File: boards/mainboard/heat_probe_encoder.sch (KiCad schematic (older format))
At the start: 27 parts, among them U1201 DB_26, U1202 DS26LV32AT, U1203 DS26LV32AT

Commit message: [mainboard] update connectors, select most footprints; docs: update SVGs
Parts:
- C1201, C1202, C1203, C1204, C1205, C1206: footprint (none) -> Capacitors_SMD:C_0603
- R1201, R1202, R1203, R1204, R1205, R1206, R1207, R1208, R1209, R1210, R1211, R1212, R1213, R1214, R1215, R1216, R1217, R1218: footprint (none) -> Resistors_SMD:R_0603
- U1202, U1203: footprint (none) -> Housings_SOIC:SOIC-16_3.9x9.9mm_Pitch1.27mm
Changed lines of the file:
@@
 $EndDescr
 $Comp
-L GND #PWR1202
+L GND #PWR0119
 U 1 1 591E0FA6
 P 1650 4900
-F 0 "#PWR1202" H 1650 4650 50  0001 C CNN
+F 0 "#PWR0119" H 1650 4650 50  0001 C CNN
 F 1 "GND" H 1650 4750 50  0000 C CNN
 F 2 "" H 1650 4900 50  0001 C CNN
@@
 F 0 "R1213" V 8080 2400 50  0000 C CNN
 F 1 "100" V 8000 2400 50  0000 C CNN
-F 2 "" V 7930 2400 50  0001 C CNN
+F 2 "Resistors_SMD:R_0603" V 7930 2400 50  0001 C CNN
 F 3 "" H 8000 2400 50  0001 C CNN
 	1    8000 2400
@@
 F 0 "R1214" V 8080 2600 50  0000 C CNN
 F 1 "100" V 8000 2600 50  0000 C CNN
-F 2 "" V 7930 2600 50  0001 C CNN
+F 2 "Resistors_SMD:R_0603" V 7930 2600 50  0001 C CNN
 F 3 "" H 8000 2600 50  0001 C CNN
 	1    8000 2600
@@
 F 0 "R1215" V 8080 2800 50  0000 C CNN
 F 1 "100" V 8000 2800 50  0000 C CNN
-F 2 "" V 7930 2800 50  0001 C CNN
+F 2 "Resistors_SMD:R_0603" V 7930 2800 50  0001 C CNN
 F 3 "" H 8000 2800 50  0001 C CNN
 	1    8000 2800
@@
 F 0 "R1216" V 8080 3000 50  0000 C CNN
 F 1 "100" V 8000 3000 50  0000 C CNN
-F 2 "" V 7930 3000 50  0001 C CNN
+F 2 "Resistors_SMD:R_0603" V 7930 3000 50  0001 C CNN
 F 3 "" H 8000 3000 50  0001 C CNN
 	1    8000 3000
@@
 F 0 "R1217" V 8080 3200 50  0000 C CNN
 F 1 "100" V 8000 3200 50  0000 C CNN
-F 2 "" V 7930 3200 50  0001 C CNN
+F 2 "Resistors_SMD:R_0603" V 7930 3200 50  0001 C CNN
 F 3 "" H 8000 3200 50  0001 C CNN
 	1    8000 3200
@@
 F 0 "R1218" V 8080 3400 50  0000 C CNN
 F 1 "100" V 8000 3400 50  0000 C CNN
-F 2 "" V 7930 3400 50  0001 C CNN
+F 2 "Resistors_SMD:R_0603" V 7930 3400 50  0001 C CNN
 F 3 "" H 8000 3400 50  0001 C CNN
 	1    8000 3400
@@
 F 0 "C1201" H 8325 3800 50  0000 L CNN
 F 1 "2n7" H 8325 3600 50  0000 L CNN
-F 2 "" H 8338 3550 50  0001 C CNN
+F 2 "Capacitors_SMD:C_0603" H 8338 3550 50  0001 C CNN
 F 3 "" H 8300 3700 50  0001 C CNN
 	1    8300 3700
@@
 F 0 "C1202" H 8575 3800 50  0000 L CNN
 F 1 "2n7" H 8575 3600 50  0000 L CNN
-F 2 "" H 8588 3550 50  0001 C CNN
+F 2 "Capacitors_SMD:C_0603" H 8588 3550 50  0001 C CNN
 F 3 "" H 8550 3700 50  0001 C CNN
 	1    8550 3700
@@
 F 0 "C1203" H 8825 3800 50  0000 L CNN
 F 1 "2n7" H 8825 3600 50  0000 L CNN
-F 2 "" H 8838 3550 50  0001 C CNN
+F 2 "Capacitors_SMD:C_0603" H 8838 3550 50  0001 C CNN
 F 3 "" H 8800 3700 50  0001 C CNN
 	1    8800 3700
@@
 F 0 "C1204" H 9075 3800 50  0000 L CNN
 F 1 "2n7" H 9075 3600 50  0000 L CNN
-F 2 "" H 9088 3550 50  0001 C CNN
+F 2 "Capacitors_SMD:C_0603" H 9088 3550 50  0001 C CNN
 F 3 "" H 9050 3700 50  0001 C CNN
 	1    9050 3700
@@
 F 0 "C1205" H 9325 3800 50  0000 L CNN
 F 1 "2n7" H 9325 3600 50  0000 L CNN
-F 2 "" H 9338 3550 50  0001 C CNN
+F 2 "Capacitors_SMD:C_0603" H 9338 3550 50  0001 C CNN
 F 3 "" H 9300 3700 50  0001 C CNN
 	1    9300 3700
@@
 F 0 "C1206" H 9575 3800 50  0000 L CNN
 F 1 "2n7" H 9575 3600 50  0000 L CNN
-F 2 "" H 9588 3550 50  0001 C CNN
+F 2 "Capacitors_SMD:C_0603" H 9588 3550 50  0001 C CNN
 F 3 "" H 9550 3700 50  0001 C CNN
 	1    9550 3700
@@
 $EndComp
 $Comp
-L GND #PWR1212
+L GND #PWR0120
 U 1 1 591E1E04
 P 8300 4050
-F 0 "#PWR1212" H 8300 3800 50  0001 C CNN
+F 0 "#PWR0120" H 8300 3800 50  0001 C CNN
 F 1 "GND" H 8300 3900 50  0000 C CNN
 F 2 "" H 8300 4050 50  0001 C CNN
@@
 F 0 "R1212" V 7480 2050 50  0000 C CNN
 F 1 "2k7" V 7400 2050 50  0000 C CNN
-F 2 "" V 7330 2050 50  0001 C CNN
+F 2 "Resistors_SMD:R_0603" V 7330 2050 50  0001 C CNN
 F 3 "" H 7400 2050 50  0001 C CNN
 	1    7400 2050
@@
 F 0 "R1211" V 7280 2050 50  0000 C CNN
 F 1 "2k7" V 7200 2050 50  0000 C CNN
-F 2 "" V 7130 2050 50  0001 C CNN
+F 2 "Resistors_SMD:R_0603" V 7130 2050 50  0001 C CNN
 F 3 "" H 7200 2050 50  0001 C CNN
 	1    7200 2050
@@
 F 0 "R1210" V 7080 2050 50  0000 C CNN
 F 1 "2k7" V 7000 2050 50  0000 C CNN
-F 2 "" V 6930 2050 50  0001 C CNN
+F 2 "Resistors_SMD:R_0603" V 6930 2050 50  0001 C CNN
 F 3 "" H 7000 2050 50  0001 C CNN
 	1    7000 2050
@@
 F 0 "R1209" V 6880 2050 50  0000 C CNN
 F 1 "2k7" V 6800 2050 50  0000 C CNN
-F 2 "" V 6730 2050 50  0001 C CNN
+F 2 "Resistors_SMD:R_0603" V 6730 2050 50  0001 C CNN
 F 3 "" H 6800 2050 50  0001 C CNN
 	1    6800 2050
@@
 F 0 "R1208" V 6680 2050 50  0000 C CNN
 F 1 "2k7" V 6600 2050 50  0000 C CNN
-F 2 "" V 6530 2050 50  0001 C CNN
+F 2 "Resistors_SMD:R_0603" V 6530 2050 50  0001 C CNN
 F 3 "" H 6600 2050 50  0001 C CNN
 	1    6600 2050
@@
 F 0 "R1207" V 6480 2050 50  0000 C CNN
 F 1 "2k7" V 6400 2050 50  0000 C CNN
-F 2 "" V 6330 2050 50  0001 C CNN
+F 2 "Resistors_SMD:R_0603" V 6330 2050 50  0001 C CNN
 F 3 "" H 6400 2050 50  0001 C CNN
 	1    6400 2050
@@
 $EndComp
 $Comp
-L +3V3 #PWR1211
+L +3V3 #PWR0121
 U 1 1 591E2628
 P 6900 1700
-F 0 "#PWR1211" H 6900 1550 50  0001 C CNN
+F 0 "#PWR0121" H 6900 1550 50  0001 C CNN
 F 1 "+3V3" H 6900 1840 50  0000 C CNN
 F 2 "" H 6900 1700 50  0001 C CNN
@@
 F 0 "U1202" H 5450 3550 60  0000 C CNN
 F 1 "DS26LV32AT" H 5450 4650 60  0000 C CNN
-F 2 "" H 5550 3900 60  0001 C CNN
+F 2 "Housings_SOIC:SOIC-16_3.9x9.9mm_Pitch1.27mm" H 5550 3900 60  0001 C CNN
 F 3 "" H 5550 3900 60  0001 C CNN
 	1    5450 4100
@@
 $EndComp
 $Comp
-L +5V #PWR1201
+L +5V #PWR0122
 U 1 1 591E0FAC
 P 1550 1900
-F 0 "#PWR1201" H 1550 1750 50  0001 C CNN
+F 0 "#PWR0122" H 1550 1750 50  0001 C CNN
 F 1 "+5V" H 1550 2040 50  0000 C CNN
 F 2 "" H 1550 1900 50  0000 C CNN
@@
 F 0 "R1201" V 4680 2400 50  0000 C CNN
 F 1 "0" V 4600 2400 50  0000 C CNN
-F 2 "" V 4530 2400 50  0001 C CNN
+F 2 "Resistors_SMD:R_0603" V 4530 2400 50  0001 C CNN
 F 3 "" H 4600 2400 50  0001 C CNN
 	1    4600 2400
@@
 F 0 "R1202" V 4680 2600 50  0000 C CNN
 F 1 "0" V 4600 2600 50  0000 C CNN
-F 2 "" V 4530 2600 50  0001 C CNN
+F 2 "Resistors_SMD:R_0603" V 4530 2600 50  0001 C CNN
 F 3 "" H 4600 2600 50  0001 C CNN
 	1    4600 2600
@@
 F 0 "R1203" V 4680 2800 50  0000 C CNN
 F 1 "0" V 4600 2800 50  0000 C CNN
-F 2 "" V 4530 2800 50  0001 C CNN
+F 2 "Resistors_SMD:R_0603" V 4530 2800 50  0001 C CNN
 F 3 "" H 4600 2800 50  0001 C CNN
 	1    4600 2800
@@
 F 0 "R1204" V 4680 3000 50  0000 C CNN
 F 1 "0" V 4600 3000 50  0000 C CNN
-F 2 "" V 4530 3000 50  0001 C CNN
+F 2 "Resistors_SMD:R_0603" V 4530 3000 50  0001 C CNN
 F 3 "" H 4600 3000 50  0001 C CNN
 	1    4600 3000
@@
 F 0 "R1205" V 4680 3200 50  0000 C CNN
 F 1 "0" V 4600 3200 50  0000 C CNN
-F 2 "" V 4530 3200 50  0001 C CNN
+F 2 "Resistors_SMD:R_0603" V 4530 3200 50  0001 C CNN
 F 3 "" H 4600 3200 50  0001 C CNN
 	1    4600 3200
@@
 F 0 "R1206" V 4680 3400 50  0000 C CNN
 F 1 "0" V 4600 3400 50  0000 C CNN
-F 2 "" V 4530 3400 50  0001 C CNN
+F 2 "Resistors_SMD:R_0603" V 4530 3400 50  0001 C CNN
 F 3 "" H 4600 3400 50  0001 C CNN
 	1    4600 3400
@@
 $EndComp
 $Comp
-L +3V3 #PWR1207
+L +3V3 #PWR0123
 U 1 1 591F1091
 P 6050 4450
-F 0 "#PWR1207" H 6050 4300 50  0001 C CNN
+F 0 "#PWR0123" H 6050 4300 50  0001 C CNN
 F 1 "+3V3" H 6050 4590 50  0000 C CNN
 F 2 "" H 6050 4450 50  0001 C CNN
@@
 $EndComp
 $Comp
-L GND #PWR1208
+L GND #PWR0124
 U 1 1 591F1111
 P 6050 4650
-F 0 "#PWR1208" H 6050 4400 50  0001 C CNN
+F 0 "#PWR0124" H 6050 4400 50  0001 C CNN
 F 1 "GND" H 6050 4500 50  0000 C CNN
 F 2 "" H 6050 4650 50  0001 C CNN
@@
 $EndComp
 $Comp
-L GND #PWR1204
+L GND #PWR0125
 U 1 1 591F1174
 P 4850 4650
-F 0 "#PWR1204" H 4850 4400 50  0001 C CNN
+F 0 "#PWR0125" H 4850 4400 50  0001 C CNN
 F 1 "GND" H 4850 4500 50  0000 C CNN
 F 2 "" H 4850 4650 50  0001 C CNN
@@
 $EndComp
 $Comp
-L +3V3 #PWR1203
+L +3V3 #PWR0126
 U 1 1 591F11D0
 P 4850 4450
-F 0 "#PWR1203" H 4850 4300 50  0001 C CNN
+F 0 "#PWR0126" H 4850 4300 50  0001 C CNN
 F 1 "+3V3" H 4850 4590 50  0000 C CNN
 F 2 "" H 4850 4450 50  0001 C CNN
@@
 F 0 "U1203" H 5450 5000 60  0000 C CNN
 F 1 "DS26LV32AT" H 5450 6100 60  0000 C CNN
-F 2 "" H 5550 5350 60  0001 C CNN
+F 2 "Housings_SOIC:SOIC-16_3.9x9.9mm_Pitch1.27mm" H 5550 5350 60  0001 C CNN
 F 3 "" H 5550 5350 60  0001 C CNN
 	1    5450 5550
@@
 Connection ~ 3100 3400
 $Comp
-L GND #PWR1206
+L GND #PWR0127
 U 1 1 591F578A
 P 4850 6100
-F 0 "#PWR1206" H 4850 5850 50  0001 C CNN
+F 0 "#PWR0127" H 4850 5850 50  0001 C CNN
 F 1 "GND" H 4850 5950 50  0000 C CNN
 F 2 "" H 4850 6100 50  0001 C CNN
@@
 $EndComp
 $Comp
-L +3V3 #PWR1205
+L +3V3 #PWR0128
 U 1 1 591F5790
 P 4850 5900
-F 0 "#PWR1205" H 4850 5750 50  0001 C CNN
+F 0 "#PWR0128" H 4850 5750 50  0001 C CNN
 F 1 "+3V3" H 4850 6040 50  0000 C CNN
 F 2 "" H 4850 5900 50  0001 C CNN
@@
 	4850 6000 4850 6100
 $Comp
-L +3V3 #PWR1209
+L +3V3 #PWR0129
 U 1 1 591F5B8B
 P 6050 5900
-F 0 "#PWR1209" H 6050 5750 50  0001 C CNN
+F 0 "#PWR0129" H 6050 5750 50  0001 C CNN
 F 1 "+3V3" H 6050 6040 50  0000 C CNN
 F 2 "" H 6050 5900 50  0001 C CNN
@@
 $EndComp
 $Comp
-L GND #PWR1210
+L GND #PWR0130
 U 1 1 591F5B91
 P 6050 6100
-F 0 "#PWR1210" H 6050 5850 50  0001 C CNN
+F 0 "#PWR0130" H 6050 5850 50  0001 C CNN
 F 1 "GND" H 6050 5950 50  0000 C CNN
 F 2 "" H 6050 6100 50  0001 C CNN

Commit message: [mainboard] layout: footprints assigned, first placement
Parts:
- U1201: value DB_26 -> Heat probe encoder; footprint (none) -> D-Sub-HD:D-Sub_HD_26_F
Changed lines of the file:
@@
 $EndDescr
 $Comp
-L GND #PWR0119
+L GND #PWR0117
 U 1 1 591E0FA6
 P 1650 4900
-F 0 "#PWR0119" H 1650 4650 50  0001 C CNN
+F 0 "#PWR0117" H 1650 4650 50  0001 C CNN
 F 1 "GND" H 1650 4750 50  0000 C CNN
 F 2 "" H 1650 4900 50  0001 C CNN
@@
 $EndComp
 $Comp
-L GND #PWR0120
+L GND #PWR0118
 U 1 1 591E1E04
 P 8300 4050
-F 0 "#PWR0120" H 8300 3800 50  0001 C CNN
+F 0 "#PWR0118" H 8300 3800 50  0001 C CNN
 F 1 "GND" H 8300 3900 50  0000 C CNN
 F 2 "" H 8300 4050 50  0001 C CNN
@@
 $EndComp
 $Comp
-L +3V3 #PWR0121
+L +3V3 #PWR0119
 U 1 1 591E2628
 P 6900 1700
-F 0 "#PWR0121" H 6900 1550 50  0001 C CNN
+F 0 "#PWR0119" H 6900 1550 50  0001 C CNN
 F 1 "+3V3" H 6900 1840 50  0000 C CNN
 F 2 "" H 6900 1700 50  0001 C CNN
@@
 P 1050 3300
 F 0 "U1201" H 1050 1950 60  0000 C CNN
-F 1 "DB_26" H 1050 4750 60  0000 C CNN
-F 2 "" H 2250 3300 60  0001 C CNN
+F 1 "Heat probe encoder" H 1050 4750 60  0000 C CNN
+F 2 "D-Sub-HD:D-Sub_HD_26_F" H 2250 3300 60  0001 C CNN
 F 3 "" H 2250 3300 60  0001 C CNN
 	1    1050 3300
@@
 $EndComp
 $Comp
-L +5V #PWR0122
+L +5V #PWR0120
 U 1 1 591E0FAC
 P 1550 1900
-F 0 "#PWR0122" H 1550 1750 50  0001 C CNN
+F 0 "#PWR0120" H 1550 1750 50  0001 C CNN
 F 1 "+5V" H 1550 2040 50  0000 C CNN
 F 2 "" H 1550 1900 50  0000 C CNN
@@
 $EndComp
 $Comp
-L +3V3 #PWR0123
+L +3V3 #PWR0121
 U 1 1 591F1091
 P 6050 4450
-F 0 "#PWR0123" H 6050 4300 50  0001 C CNN
+F 0 "#PWR0121" H 6050 4300 50  0001 C CNN
 F 1 "+3V3" H 6050 4590 50  0000 C CNN
 F 2 "" H 6050 4450 50  0001 C CNN
@@
 $EndComp
 $Comp
-L GND #PWR0124
+L GND #PWR0122
 U 1 1 591F1111
 P 6050 4650
-F 0 "#PWR0124" H 6050 4400 50  0001 C CNN
+F 0 "#PWR0122" H 6050 4400 50  0001 C CNN
 F 1 "GND" H 6050 4500 50  0000 C CNN
 F 2 "" H 6050 4650 50  0001 C CNN
@@
 $EndComp
 $Comp
-L GND #PWR0125
+L GND #PWR0123
 U 1 1 591F1174
 P 4850 4650
-F 0 "#PWR0125" H 4850 4400 50  0001 C CNN
+F 0 "#PWR0123" H 4850 4400 50  0001 C CNN
 F 1 "GND" H 4850 4500 50  0000 C CNN
 F 2 "" H 4850 4650 50  0001 C CNN
@@
 $EndComp
 $Comp
-L +3V3 #PWR0126
+L +3V3 #PWR0124
 U 1 1 591F11D0
 P 4850 4450
-F 0 "#PWR0126" H 4850 4300 50  0001 C CNN
+F 0 "#PWR0124" H 4850 4300 50  0001 C CNN
 F 1 "+3V3" H 4850 4590 50  0000 C CNN
 F 2 "" H 4850 4450 50  0001 C CNN
@@
 Connection ~ 3100 3400
 $Comp
-L GND #PWR0127
+L GND #PWR0125
 U 1 1 591F578A
 P 4850 6100
-F 0 "#PWR0127" H 4850 5850 50  0001 C CNN
+F 0 "#PWR0125" H 4850 5850 50  0001 C CNN
 F 1 "GND" H 4850 5950 50  0000 C CNN
 F 2 "" H 4850 6100 50  0001 C CNN
@@
 $EndComp
 $Comp
-L +3V3 #PWR0128
+L +3V3 #PWR0126
 U 1 1 591F5790
 P 4850 5900
-F 0 "#PWR0128" H 4850 5750 50  0001 C CNN
+F 0 "#PWR0126" H 4850 5750 50  0001 C CNN
 F 1 "+3V3" H 4850 6040 50  0000 C CNN
 F 2 "" H 4850 5900 50  0001 C CNN
@@
 	4850 6000 4850 6100
 $Comp
-L +3V3 #PWR0129
+L +3V3 #PWR0127
 U 1 1 591F5B8B
 P 6050 5900
-F 0 "#PWR0129" H 6050 5750 50  0001 C CNN
+F 0 "#PWR0127" H 6050 5750 50  0001 C CNN
 F 1 "+3V3" H 6050 6040 50  0000 C CNN
 F 2 "" H 6050 5900 50  0001 C CNN
@@
 $EndComp
 $Comp
-L GND #PWR0130
+L GND #PWR0128
 U 1 1 591F5B91
 P 6050 6100
-F 0 "#PWR0130" H 6050 5850 50  0001 C CNN
+F 0 "#PWR0128" H 6050 5850 50  0001 C CNN
 F 1 "GND" H 6050 5950 50  0000 C CNN
 F 2 "" H 6050 6100 50  0001 C CNN

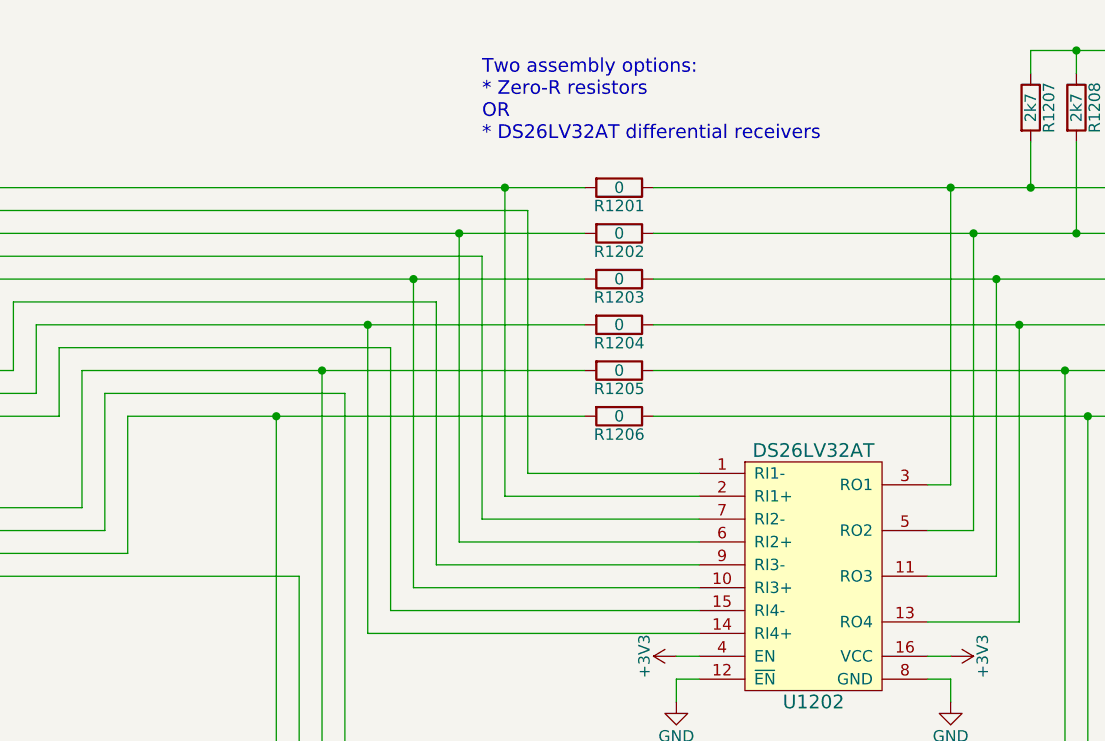
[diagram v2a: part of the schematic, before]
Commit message: [mainboard] layout: footprint placement
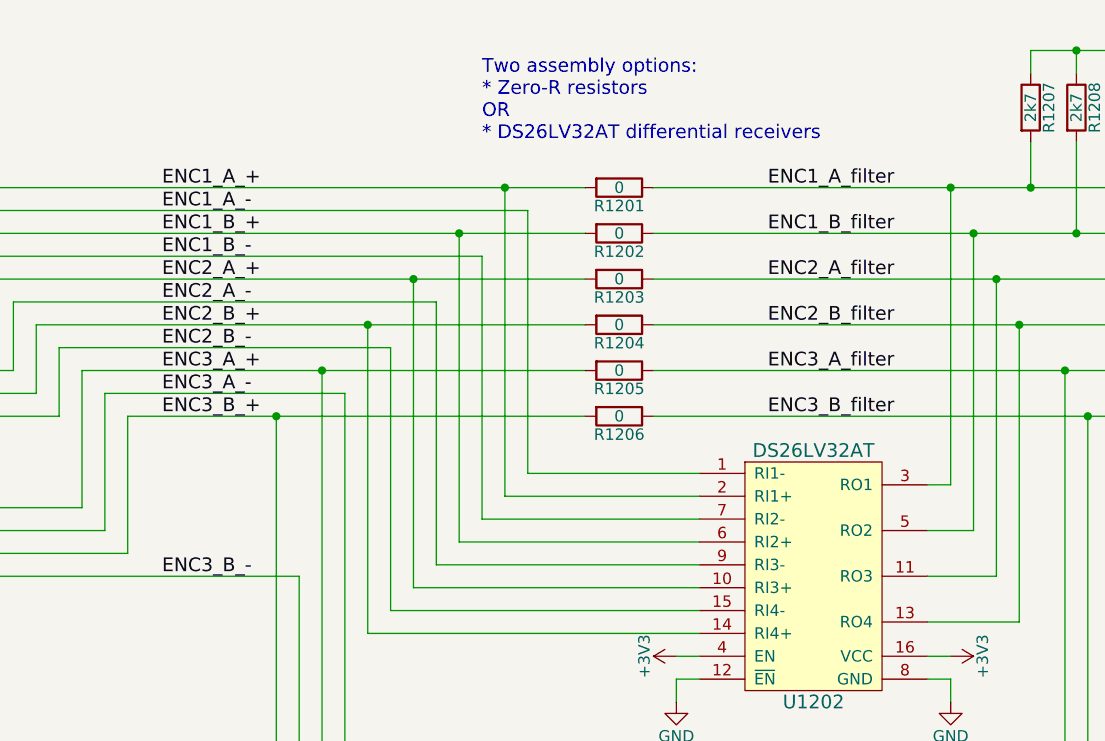
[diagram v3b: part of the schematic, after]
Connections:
- net ENC1_A_filter: now reaches R1201.1, R1207.2, R1213.2, U1202.3 (RO1)
- net ENC1_B_filter: now reaches R1202.1, R1208.2, R1214.2, U1202.5 (RO2)
- net ENC2_A_filter: now reaches R1203.1, R1209.2, R1215.2, U1202.11 (RO3)
- net ENC2_B_filter: now reaches R1204.1, R1210.2, R1216.2, U1202.13 (RO4)
- net ENC3_A_filter: now reaches R1205.1, R1211.2, R1217.2, U1203.3 (RO1)
- net ENC3_B_filter: now reaches R1206.1, R1212.2, R1218.2, U1203.5 (RO2)
- net ENC1_A_-: now reaches U1201.20, U1202.1 (RI1-)
- net ENC2_A_+: now reaches R1203.2, U1201.22, U1202.10 (RI3+)
- net ENC2_B_+: now reaches R1204.2, U1201.5, U1202.14 (RI4+)
- net ENC2_B_-: now reaches U1201.23, U1202.15 (RI4-)
- net ENC1_A_+: now reaches R1201.2, U1201.2, U1202.2 (RI1+)
- net ENC1_B_+: now reaches R1202.2, U1201.12, U1202.6 (RI2+)
- net ENC1_B_-: now reaches U1201.3, U1202.7 (RI2-)
- net ENC2_A_-: now reaches U1201.14, U1202.9 (RI3-)
- net ENC3_A_+: now reaches R1205.2, U1201.16, U1203.2 (RI1+)
- net ENC3_B_-: now reaches U1201.17, U1203.7 (RI2-)
- net ENC3_B_+: now reaches R1206.2, U1201.25, U1203.6 (RI2+)
- net ENC3_A_-: now reaches U1201.7, U1203.1 (RI1-)
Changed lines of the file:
@@
 Text Notes 4000 2200 0    60   ~ 0
 Two assembly options:\n* Zero-R resistors\nOR\n* DS26LV32AT differential receivers
+Text Label 2600 2400 0    60   ~ 0
+ENC1_A_+
+Text Label 2600 2500 0    60   ~ 0
+ENC1_A_-
+Text Label 2600 2600 0    60   ~ 0
+ENC1_B_+
+Text Label 2600 2700 0    60   ~ 0
+ENC1_B_-
+Text Label 2600 2800 0    60   ~ 0
+ENC2_A_+
+Text Label 2600 2900 0    60   ~ 0
+ENC2_A_-
+Text Label 2600 3000 0    60   ~ 0
+ENC2_B_+
+Text Label 2600 3100 0    60   ~ 0
+ENC2_B_-
+Text Label 2600 3200 0    60   ~ 0
+ENC3_A_+
+Text Label 2600 3300 0    60   ~ 0
+ENC3_A_-
+Text Label 2600 3400 0    60   ~ 0
+ENC3_B_+
+Text Label 2600 4100 0    60   ~ 0
+ENC3_B_-
+Text Label 5250 2400 0    60   ~ 0
+ENC1_A_filter
+Text Label 5250 2600 0    60   ~ 0
+ENC1_B_filter
+Text Label 5250 2800 0    60   ~ 0
+ENC2_A_filter
+Text Label 5250 3000 0    60   ~ 0
+ENC2_B_filter
+Text Label 5250 3200 0    60   ~ 0
+ENC3_A_filter
+Text Label 5250 3400 0    60   ~ 0
+ENC3_B_filter
 $EndSCHEMATC

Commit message: [mainboard] add test points
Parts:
- added J1201: ENC1_A, Measurement_Points:Measurement_Point_Round-SMD-Pad_Small, symbol TEST_1P
- added J1202: ENC1_B, Measurement_Points:Measurement_Point_Round-SMD-Pad_Small, symbol TEST_1P
- added J1203: ENC2_A, Measurement_Points:Measurement_Point_Round-SMD-Pad_Small, symbol TEST_1P
- added J1204: ENC2_B, Measurement_Points:Measurement_Point_Round-SMD-Pad_Small, symbol TEST_1P
- added J1205: ENC3_A, Measurement_Points:Measurement_Point_Round-SMD-Pad_Small, symbol TEST_1P
- added J1206: ENC3_B, Measurement_Points:Measurement_Point_Round-SMD-Pad_Small, symbol TEST_1P
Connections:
- net ENC1_A: now also J1201.1
- net ENC1_B: now also J1202.1
- net ENC2_A: now also J1203.1
- net ENC2_B: now also J1204.1
- net ENC3_A: now also J1205.1
- net ENC3_B: now also J1206.1
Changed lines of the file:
@@
 Text Notes 6350 1450 0    60   ~ 0
 Optional pull-ups for\nopen-drain encoder outputs
-Text Notes 8150 2250 0    60   ~ 0
+Text Notes 7800 4500 0    60   ~ 0
 Optional RC-filter to remove noise\nfrom encoder cables
 $Comp
@@
 	8150 2400 9850 2400
 Wire Wire Line
-	8300 2400 8300 3550
+	8300 2300 8300 3550
 Connection ~ 8300 2400
 Wire Wire Line
-	8550 3550 8550 2600
+	8550 2300 8550 3550
 Connection ~ 8550 2600
 Wire Wire Line
-	8800 3550 8800 2800
+	8800 2300 8800 3550
 Connection ~ 8800 2800
 Wire Wire Line
-	9050 3000 9050 3550
+	9050 2300 9050 3550
 Connection ~ 9050 3000
 Wire Wire Line
-	9300 3550 9300 3200
+	9300 2300 9300 3550
 Connection ~ 9300 3200
 Wire Wire Line
-	9550 3400 9550 3550
+	9550 2300 9550 3550
 Connection ~ 9550 3400
 Wire Wire Line
@@
 Text Label 5250 3400 0    60   ~ 0
 ENC3_B_filter
+$Comp
+L TEST_1P J1201
+U 1 1 591724E9
+P 8300 2300
+F 0 "J1201" V 8200 2450 50  0000 C CNN
+F 1 "ENC1_A" V 8300 2650 50  0000 C CNN
+F 2 "Measurement_Points:Measurement_Point_Round-SMD-Pad_Small" H 8500 2300 50  0001 C CNN
+F 3 "" H 8500 2300 50  0001 C CNN
+	1    8300 2300
+	1    0    0    -1
+$EndComp
+$Comp
+L TEST_1P J1202
+U 1 1 59172B15
+P 8550 2300
+F 0 "J1202" V 8450 2450 50  0000 C CNN
+F 1 "ENC1_B" V 8550 2650 50  0000 C CNN
+F 2 "Measurement_Points:Measurement_Point_Round-SMD-Pad_Small" H 8750 2300 50  0001 C CNN
+F 3 "" H 8750 2300 50  0001 C CNN
+	1    8550 2300
+	1    0    0    -1
+$EndComp
+$Comp
+L TEST_1P J1203
+U 1 1 59172B82
+P 8800 2300
+F 0 "J1203" V 8700 2450 50  0000 C CNN
+F 1 "ENC2_A" V 8800 2650 50  0000 C CNN
+F 2 "Measurement_Points:Measurement_Point_Round-SMD-Pad_Small" H 9000 2300 50  0001 C CNN
+F 3 "" H 9000 2300 50  0001 C CNN
+	1    8800 2300
+	1    0    0    -1
+$EndComp
+$Comp
+L TEST_1P J1204
+U 1 1 59172BF0
+P 9050 2300
+F 0 "J1204" V 8950 2450 50  0000 C CNN
+F 1 "ENC2_B" V 9050 2650 50  0000 C CNN
+F 2 "Measurement_Points:Measurement_Point_Round-SMD-Pad_Small" H 9250 2300 50  0001 C CNN
+F 3 "" H 9250 2300 50  0001 C CNN
+	1    9050 2300
+	1    0    0    -1
+$EndComp
+$Comp
+L TEST_1P J1205
+U 1 1 59173060
+P 9300 2300
+F 0 "J1205" V 9200 2450 50  0000 C CNN
+F 1 "ENC3_A" V 9300 2650 50  0000 C CNN
+F 2 "Measurement_Points:Measurement_Point_Round-SMD-Pad_Small" H 9500 2300 50  0001 C CNN
+F 3 "" H 9500 2300 50  0001 C CNN
+	1    9300 2300
+	1    0    0    -1
+$EndComp
+$Comp
+L TEST_1P J1206
+U 1 1 591730D4
+P 9550 2300
+F 0 "J1206" V 9450 2450 50  0000 C CNN
+F 1 "ENC3_B" V 9550 2650 50  0000 C CNN
+F 2 "Measurement_Points:Measurement_Point_Round-SMD-Pad_Small" H 9750 2300 50  0001 C CNN
+F 3 "" H 9750 2300 50  0001 C CNN
+	1    9550 2300
+	1    0    0    -1
+$EndComp
 $EndSCHEMATC
